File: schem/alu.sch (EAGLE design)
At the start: 10 parts, among them IC1 74HC181N, IC10 74HC08N, IC11 74HC86N, IC2 74HC181N, IC3 74HC04N, IC5 74HC244N, IC6 74HC244N, IC7 74HC32N, IC8 74HC32N, IC9 74HC86N

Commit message: updated alu schematic
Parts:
- added IC12, IC13, IC14, IC15, IC16, IC17: 74HC151N, 74xx-eu:74HC151N
- added IC18: 74HC244N, 74xx-eu:74HC244N
- added IC4: 74HC181N, 74xx-eu:74HC181N
- IC1: value 74HC181N -> 74HC244N; device 74xx-eu:74HC181N -> 74xx-eu:74HC244N
- IC11: value 74HC86N -> 74HC377N; device 74xx-eu:74HC86N -> 74xx-eu:74HC377N
- IC2: value 74HC181N -> 74HC04N; device 74xx-eu:74HC181N -> 74xx-eu:74HC04N
- IC3: value 74HC04N -> 74HC86N; device 74xx-eu:74HC04N -> 74xx-eu:74HC86N
- IC5: value 74HC244N -> 74HC181N; device 74xx-eu:74HC244N -> 74xx-eu:74HC181N
- IC7: value 74HC32N -> 74HC86N; device 74xx-eu:74HC32N -> 74xx-eu:74HC86N
- IC9: value 74HC86N -> 74HC32N; device 74xx-eu:74HC86N -> 74xx-eu:74HC32N
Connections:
- new net CLK: IC11A.CLK
- new net COND: IC17A.Y
- new net FL0: IC12A.A
- new net FL1: IC12A.B
- new net FL2: IC13A.A
- new net FL3: IC13A.B
- new net FL4: IC14A.A
- new net FL5: IC14A.B
- new net FL6: IC15A.A
- new net FL7: IC15A.B
- new net FL8: IC16A.A
- new net FL9: IC16A.B
- new net GND: IC11A.4D, IC11A.5D, IC11A.G, IC12A.D7, IC12A.G, IC13A.D7, IC13A.G, IC14A.D5, IC14A.D7, IC14A.G, IC15A.D7, IC15A.G, IC16A.D7, IC16A.G, IC17A.C, IC17A.D4, IC17A.D5, IC17A.D6, IC17A.D7, IC17A.G
- new net IBD10: IC18A.G, IC18B.G
- new net INIRQ: IC11A.6D
- new net N: IC16A.D5
- new net OBD10: IC12A.C, IC13A.C, IC14A.C, IC15A.C, IC16A.C
- new net PD0: IC11A.1D, IC12A.Y
- new net PD1: IC11A.2D, IC13A.Y
- new net PD2: IC11A.3D, IC14A.Y
- new net PD6: IC11A.7D, IC15A.Y
- new net PD7: IC11A.8D, IC16A.Y
- new net PQ0: IC11A.1Q, IC12A.D0, IC12A.D2, IC12A.D3, IC12A.D4, IC17A.D2, IC18A.A1
- new net PQ1: IC11A.2Q, IC13A.D0, IC13A.D2, IC13A.D3, IC13A.D4, IC17A.D3, IC18A.A2
- new net PQ2: IC11A.3Q, IC14A.D0, IC14A.D2, IC14A.D3, IC14A.D4, IC18A.A3
- new net PQ3: IC11A.4Q, IC18A.A4
- new net PQ4: IC11A.5Q, IC18B.A1
- new net PQ5: IC11A.6Q, IC18B.A2
- new net PQ6: IC11A.7Q, IC15A.D0, IC15A.D2, IC15A.D3, IC15A.D4, IC17A.D1, IC18B.A3
- new net PQ7: IC11A.8Q, IC16A.D0, IC16A.D2, IC16A.D3, IC16A.D4, IC17A.D0, IC18B.A4
- new net VCC: IC12A.D6, IC13A.D6, IC14A.D6, IC15A.D6, IC16A.D6
- net /CIN: now also IC2A.O, IC4A.CN; no longer IC1A.CN, IC3A.O
- net /COUTA: now also IC2B.I, IC5A.CN+4; no longer IC2A.CN+4, IC3B.I
- net /F0: now also IC2E.O, IC7A.I1; no longer IC3E.O, IC9A.I1
- net /F5: now also IC1A.G, IC1B.G, IC2C.O; no longer IC3C.O, IC6A.G, IC6B.G
- net /V1: now also IC2F.O; no longer IC3F.O
- net /Z: now also IC2D.I, IC8D.O; no longer IC3D.I, IC7D.O
- net C: now also IC12A.D5, IC9D.O; no longer IC8D.O
- net C1: now also IC9D.I0; no longer IC8D.I0
- net C2: now also IC9D.I1; no longer IC8D.I1
- net C4: now also IC4A.CN+4, IC5A.CN; no longer IC1A.CN+4, IC2A.CN
- net CIN: now also IC1B.A4, IC2A.I; no longer IC3A.I, IC6B.A4
- net COUTA: now also IC2B.O; no longer IC3B.O
- net DB0: now also IC4A.B0; no longer IC1A.B0
- net DB1: now also IC4A.B1; no longer IC1A.B1
- net DB2: now also IC4A.B2; no longer IC1A.B2
- net DB3: now also IC4A.B3; no longer IC1A.B3
- net DB4: now also IC5A.B0; no longer IC2A.B0
- net DB5: now also IC5A.B1; no longer IC2A.B1
- net DB6: now also IC17A.A, IC5A.B2; no longer IC2A.B2
- net DB7: now also IC17A.B, IC5A.B3, IC7A.I0; no longer IC2A.B3, IC9A.I0
- net F0: now also IC3A.I0; no longer IC11A.I0
- net F1: now also IC3B.I0; no longer IC11B.I0
- net F2: now also IC3C.I0; no longer IC11C.I0
- net F3: now also IC3D.I0; no longer IC11D.I0
- net F4: now also IC4A.M, IC5A.M; no longer IC1A.M, IC2A.M
- net F5: now also IC2C.I, IC6A.G, IC6B.G; no longer IC3C.I, IC5A.G, IC5B.G
- net FX0: now also IC2E.I, IC3A.O, IC4A.S0, IC5A.S0; no longer IC11A.O, IC1A.S0, IC2A.S0, IC3E.I
- net FX1: now also IC3B.O, IC4A.S1, IC5A.S1; no longer IC11B.O, IC1A.S1, IC2A.S1
- net FX2: now also IC3C.O, IC4A.S2, IC5A.S2; no longer IC11C.O, IC1A.S2, IC2A.S2
- net FX3: now also IC3D.O, IC4A.S3, IC5A.S3; no longer IC11D.O, IC1A.S3, IC2A.S3
- net IB0: now also IC18A.Y1, IC4A.A0; no longer IC1A.A0
- net IB1: now also IC18A.Y2, IC4A.A1; no longer IC6A.A1
- net IB2: now also IC18A.Y3, IC4A.A2; no longer IC6A.A2
- net IB3: now also IC18A.Y4, IC4A.A3; no longer IC6A.A3
- net IB4: now also IC18B.Y1, IC1A.A4, IC5A.A0; no longer IC2A.A0, IC6A.A4
- net IB5: now also IC18B.Y2, IC1B.A1, IC5A.A1; no longer IC2A.A1, IC6B.A1
- net IB6: now also IC18B.Y3, IC1B.A2, IC5A.A2; no longer IC2A.A2, IC6B.A2
- net IB7: now also IC18B.Y4, IC1B.A3, IC5A.A3, IC7B.I0, IC7C.I1; no longer IC2A.A3, IC6B.A3, IC9B.I0, IC9C.I1
- net INVF: now also IC3A.I1, IC3B.I1, IC3C.I1, IC3D.I1; no longer IC11A.I1, IC11B.I1, IC11C.I1, IC11D.I1
- net OB0: now also IC12A.D1, IC1A.Y1, IC8A.I0; no longer IC5A.Y1, IC7A.I0
- net OB1: now also IC13A.D1, IC1A.Y2, IC8A.I1; no longer IC5A.Y2, IC7A.I1
- net OB2: now also IC14A.D1, IC1A.Y3, IC8B.I0; no longer IC5A.Y3, IC7B.I0
- net OB3: now also IC1A.Y4, IC8B.I1; no longer IC5A.Y4, IC7B.I1
- net OB4: now also IC1B.Y1, IC9A.I0; no longer IC5B.Y1, IC8A.I0
- net OB5: now also IC1B.Y2, IC9A.I1; no longer IC5B.Y2, IC8A.I1
- net OB6: now also IC15A.D1, IC1B.Y3, IC9B.I0; no longer IC5B.Y3, IC8B.I0
- net OB7: now also IC16A.D1, IC1B.Y4, IC9B.I1; no longer IC5B.Y4, IC8B.I1
- net OBA0: now also IC4A.F0, IC6A.A1; no longer IC1A.F0, IC5A.A1
- net OBA1: now also IC4A.F1, IC6A.A2; no longer IC1A.F1, IC5A.A2
- net OBA2: now also IC4A.F2, IC6A.A3; no longer IC1A.F2, IC5A.A3
- net OBA3: now also IC4A.F3, IC6A.A4; no longer IC1A.F3, IC5A.A4
- net OBA4: now also IC5A.F0, IC6B.A1; no longer IC2A.F0, IC5B.A1
- net OBA5: now also IC5A.F1, IC6B.A2; no longer IC2A.F1, IC5B.A2
- net OBA6: now also IC5A.F2, IC6B.A3; no longer IC2A.F2, IC5B.A3
- net OBA7: now also IC5A.F3, IC6B.A4, IC7C.I0; no longer IC2A.F3, IC5B.A4, IC9C.I0
- net V: now also IC15A.D5
- net V0: now also IC7A.O, IC7B.I1; no longer IC9A.O, IC9B.I1
- net V1: now also IC2F.I, IC7B.O; no longer IC3F.I, IC9B.O
- net V2: now also IC7C.O; no longer IC9C.O
- net Z: now also IC13A.D5, IC2D.O; no longer IC3D.O
- net Z0: now also IC8A.O, IC8C.I0; no longer IC7A.O, IC7C.I0
- net Z1: now also IC8B.O, IC8C.I1; no longer IC7B.O, IC7C.I1
- net Z2: now also IC9A.O, IC9C.I0; no longer IC8A.O, IC8C.I0
- net Z3: now also IC9B.O, IC9C.I1; no longer IC8B.O, IC8C.I1
- net Z4: now also IC8C.O, IC8D.I0; no longer IC7C.O, IC7D.I0
- net Z5: now also IC8D.I1, IC9C.O; no longer IC7D.I1, IC8C.O
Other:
- moved on the sheet: IC6A, IC6B, IC8A, IC8B, IC8C, IC8D

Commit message: rom and misc board schematics
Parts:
- IC1: value 74HC244N -> 74HC181N; device 74xx-eu:74HC244N -> 74xx-eu:74HC181N
- IC11: value 74HC377N -> 74HC151N; device 74xx-eu:74HC377N -> 74xx-eu:74HC151N
- IC14: value 74HC151N -> 74HC244N; device 74xx-eu:74HC151N -> 74xx-eu:74HC244N
- IC18: value 74HC244N -> 74HC377N; device 74xx-eu:74HC244N -> 74xx-eu:74HC377N
- IC2: value 74HC04N -> 74HC181N; device 74xx-eu:74HC04N -> 74xx-eu:74HC181N
- IC3: value 74HC86N -> 74HC04N; device 74xx-eu:74HC86N -> 74xx-eu:74HC04N
- IC4: value 74HC181N -> 74HC244N; device 74xx-eu:74HC181N -> 74xx-eu:74HC244N
- IC5: value 74HC181N -> 74HC32N; device 74xx-eu:74HC181N -> 74xx-eu:74HC32N
- IC6: value 74HC244N -> 74HC86N; device 74xx-eu:74HC244N -> 74xx-eu:74HC86N
- IC8: value 74HC32N -> 74HC244N; device 74xx-eu:74HC32N -> 74xx-eu:74HC244N
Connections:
- net /CIN: now also IC1A.CN, IC3A.O; no longer IC2A.O, IC4A.CN
- net /COUTA: now also IC2A.CN+4, IC3B.I; no longer IC2B.I, IC5A.CN+4
- net /F0: now also IC3E.O, IC6A.I1; no longer IC2E.O, IC7A.I1
- net /F5: now also IC3C.O, IC8A.G, IC8B.G; no longer IC1A.G, IC1B.G, IC2C.O
- net /V1: now also IC3F.O; no longer IC2F.O
- net /Z: now also IC3D.I, IC5D.O; no longer IC2D.I, IC8D.O
- net C: now also IC11A.D5; no longer IC12A.D5
- net C4: now also IC1A.CN+4, IC2A.CN; no longer IC4A.CN+4, IC5A.CN
- net CIN: now also IC3A.I, IC8B.A4; no longer IC1B.A4, IC2A.I
- net CLK: now also IC18A.CLK; no longer IC11A.CLK
- net COUTA: now also IC3B.O; no longer IC2B.O
- net DB0: now also IC1A.B0; no longer IC4A.B0
- net DB1: now also IC1A.B1; no longer IC4A.B1
- net DB2: now also IC1A.B2; no longer IC4A.B2
- net DB3: now also IC1A.B3; no longer IC4A.B3
- net DB4: now also IC2A.B0; no longer IC5A.B0
- net DB5: now also IC2A.B1; no longer IC5A.B1
- net DB6: now also IC2A.B2; no longer IC5A.B2
- net DB7: now also IC2A.B3, IC6A.I0; no longer IC5A.B3, IC7A.I0
- net F0: now also IC7A.I0; no longer IC3A.I0
- net F1: now also IC7B.I0; no longer IC3B.I0
- net F2: now also IC7C.I0; no longer IC3C.I0
- net F3: now also IC7D.I0; no longer IC3D.I0
- net F4: now also IC1A.M, IC2A.M; no longer IC4A.M, IC5A.M
- net F5: now also IC3C.I, IC4A.G, IC4B.G; no longer IC2C.I, IC6A.G, IC6B.G
- net FL0: now also IC11A.A; no longer IC12A.A
- net FL1: now also IC11A.B; no longer IC12A.B
- net FL2: now also IC12A.A; no longer IC13A.A
- net FL3: now also IC12A.B; no longer IC13A.B
- net FL4: now also IC13A.A; no longer IC14A.A
- net FL5: now also IC13A.B; no longer IC14A.B
- net FX0: now also IC1A.S0, IC2A.S0, IC3E.I, IC7A.O; no longer IC2E.I, IC3A.O, IC4A.S0, IC5A.S0
- net FX1: now also IC1A.S1, IC2A.S1, IC7B.O; no longer IC3B.O, IC4A.S1, IC5A.S1
- net FX2: now also IC1A.S2, IC2A.S2, IC7C.O; no longer IC3C.O, IC4A.S2, IC5A.S2
- net FX3: now also IC1A.S3, IC2A.S3, IC7D.O; no longer IC3D.O, IC4A.S3, IC5A.S3
- net GND: now also IC11A.D7, IC13A.D5, IC18A.4D, IC18A.5D, IC18A.G; no longer IC11A.4D, IC11A.5D, IC14A.D5, IC14A.D7, IC14A.G
- net IB0: now also IC14A.Y1, IC1A.A0; no longer IC18A.Y1, IC4A.A0
- net IB1: now also IC14A.Y2, IC8A.A1; no longer IC18A.Y2, IC4A.A1
- net IB2: now also IC14A.Y3, IC8A.A2; no longer IC18A.Y3, IC4A.A2
- net IB3: now also IC14A.Y4, IC8A.A3; no longer IC18A.Y4, IC4A.A3
- net IB4: now also IC14B.Y1, IC2A.A0, IC8A.A4; no longer IC18B.Y1, IC1A.A4, IC5A.A0
- net IB5: now also IC14B.Y2, IC2A.A1, IC8B.A1; no longer IC18B.Y2, IC1B.A1, IC5A.A1
- net IB6: now also IC14B.Y3, IC2A.A2, IC8B.A2; no longer IC18B.Y3, IC1B.A2, IC5A.A2
- net IB7: now also IC14B.Y4, IC2A.A3, IC6B.I0, IC6C.I1, IC8B.A3; no longer IC18B.Y4, IC1B.A3, IC5A.A3, IC7B.I0, IC7C.I1
- net IBD10: now also IC14A.G, IC14B.G; no longer IC18A.G, IC18B.G
- net INIRQ: now also IC18A.6D; no longer IC11A.6D
- net INVF: now also IC7A.I1, IC7B.I1, IC7C.I1, IC7D.I1; no longer IC3A.I1, IC3B.I1, IC3C.I1, IC3D.I1
- net OB0: now also IC11A.D1, IC4A.Y1, IC5A.I0, IC8A.Y1; no longer IC12A.D1, IC1A.Y1, IC6A.Y1, IC8A.I0
- net OB1: now also IC12A.D1, IC4A.Y2, IC5A.I1, IC8A.Y2; no longer IC13A.D1, IC1A.Y2, IC6A.Y2, IC8A.I1
- net OB2: now also IC13A.D1, IC4A.Y3, IC5B.I0, IC8A.Y3; no longer IC14A.D1, IC1A.Y3, IC6A.Y3, IC8B.I0
- net OB3: now also IC4A.Y4, IC5B.I1, IC8A.Y4; no longer IC1A.Y4, IC6A.Y4, IC8B.I1
- net OB4: now also IC4B.Y1, IC8B.Y1; no longer IC1B.Y1, IC6B.Y1
- net OB5: now also IC4B.Y2, IC8B.Y2; no longer IC1B.Y2, IC6B.Y2
- net OB6: now also IC4B.Y3, IC8B.Y3; no longer IC1B.Y3, IC6B.Y3
- net OB7: now also IC4B.Y4, IC8B.Y4; no longer IC1B.Y4, IC6B.Y4
- net OBA0: now also IC1A.F0, IC4A.A1; no longer IC4A.F0, IC6A.A1
- net OBA1: now also IC1A.F1, IC4A.A2; no longer IC4A.F1, IC6A.A2
- net OBA2: now also IC1A.F2, IC4A.A3; no longer IC4A.F2, IC6A.A3
- net OBA3: now also IC1A.F3, IC4A.A4; no longer IC4A.F3, IC6A.A4
- net OBA4: now also IC2A.F0, IC4B.A1; no longer IC5A.F0, IC6B.A1
- net OBA5: now also IC2A.F1, IC4B.A2; no longer IC5A.F1, IC6B.A2
- net OBA6: now also IC2A.F2, IC4B.A3; no longer IC5A.F2, IC6B.A3
- net OBA7: now also IC2A.F3, IC4B.A4, IC6C.I0; no longer IC5A.F3, IC6B.A4, IC7C.I0
- net OBD10: now also IC11A.C; no longer IC14A.C
- net PD0: now also IC11A.Y, IC18A.1D; no longer IC11A.1D, IC12A.Y
- net PD1: now also IC12A.Y, IC18A.2D; no longer IC11A.2D, IC13A.Y
- net PD2: now also IC13A.Y, IC18A.3D; no longer IC11A.3D, IC14A.Y
- net PD6: now also IC18A.7D; no longer IC11A.7D
- net PD7: now also IC18A.8D; no longer IC11A.8D
- net PQ0: now also IC11A.D0, IC11A.D2, IC11A.D3, IC11A.D4, IC14A.A1, IC18A.1Q; no longer IC11A.1Q, IC12A.D0, IC12A.D2, IC12A.D3, IC12A.D4, IC18A.A1
- net PQ1: now also IC12A.D0, IC12A.D2, IC12A.D3, IC12A.D4, IC14A.A2, IC18A.2Q; no longer IC11A.2Q, IC13A.D0, IC13A.D2, IC13A.D3, IC13A.D4, IC18A.A2
- net PQ2: now also IC13A.D0, IC13A.D2, IC13A.D3, IC13A.D4, IC14A.A3, IC18A.3Q; no longer IC11A.3Q, IC14A.D0, IC14A.D2, IC14A.D3, IC14A.D4, IC18A.A3
- net PQ3: now also IC14A.A4, IC18A.4Q; no longer IC11A.4Q, IC18A.A4
- net PQ4: now also IC14B.A1, IC18A.5Q; no longer IC11A.5Q, IC18B.A1
- net PQ5: now also IC14B.A2, IC18A.6Q; no longer IC11A.6Q, IC18B.A2
- net PQ6: now also IC14B.A3, IC18A.7Q; no longer IC11A.7Q, IC18B.A3
- net PQ7: now also IC14B.A4, IC18A.8Q; no longer IC11A.8Q, IC18B.A4
- net V0: now also IC6A.O, IC6B.I1; no longer IC7A.O, IC7B.I1
- net V1: now also IC3F.I, IC6B.O; no longer IC2F.I, IC7B.O
- net V2: now also IC6C.O; no longer IC7C.O
- net VCC: now also IC11A.D6; no longer IC14A.D6
- net Z: now also IC12A.D5, IC3D.O; no longer IC13A.D5, IC2D.O
- net Z0: now also IC5A.O, IC5C.I0; no longer IC8A.O, IC8C.I0
- net Z1: now also IC5B.O, IC5C.I1; no longer IC8B.O, IC8C.I1
- net Z4: now also IC5C.O, IC5D.I0; no longer IC8C.O, IC8D.I0
- net Z5: now also IC5D.I1; no longer IC8D.I1
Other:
- moved on the sheet: IC12, IC13, IC7A, IC7B, IC7C

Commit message: progress
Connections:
- net C renamed ALUC
- removed net N: IC16A.D5
- net OB7: now also IC16A.D5
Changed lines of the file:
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@@
 <label x="299.72" y="48.26" size="1.778" layer="95"/>
+</segment>
+<segment>
+<pinref part="IC16" gate="A" pin="D5"/>
+<wire x1="304.8" y1="38.1" x2="299.72" y2="38.1" width="0.1524" layer="91"/>
+<label x="299.72" y="38.1" size="1.778" layer="95"/>
 </segment>
 </net>
@@
 </segment>
 </net>
-<net name="C" class="0">
+<net name="ALUC" class="0">
 <segment>
 <pinref part="IC9" gate="D" pin="O"/>
@@
 </segment>
 </net>
-<net name="N" class="0">
-<segment>
-<pinref part="IC16" gate="A" pin="D5"/>
-<wire x1="304.8" y1="38.1" x2="299.72" y2="38.1" width="0.1524" layer="91"/>
-<label x="299.72" y="38.1" size="1.778" layer="95"/>
-</segment>
-</net>
 <net name="FL8" class="0">
 <segment>
@@
 </sheet>
 </sheets>
+<errors>
+</errors>
 </schematic>
 </drawing>

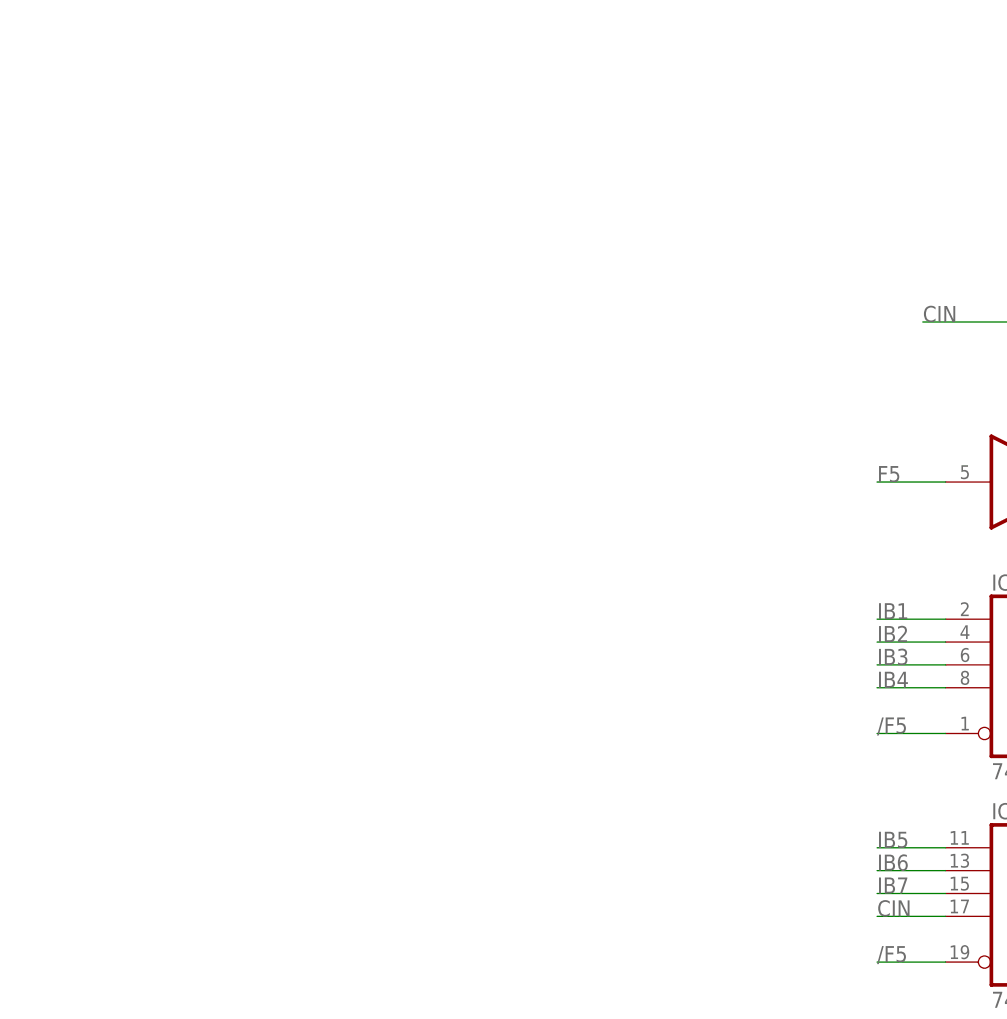
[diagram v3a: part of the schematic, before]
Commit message: connector layout changes
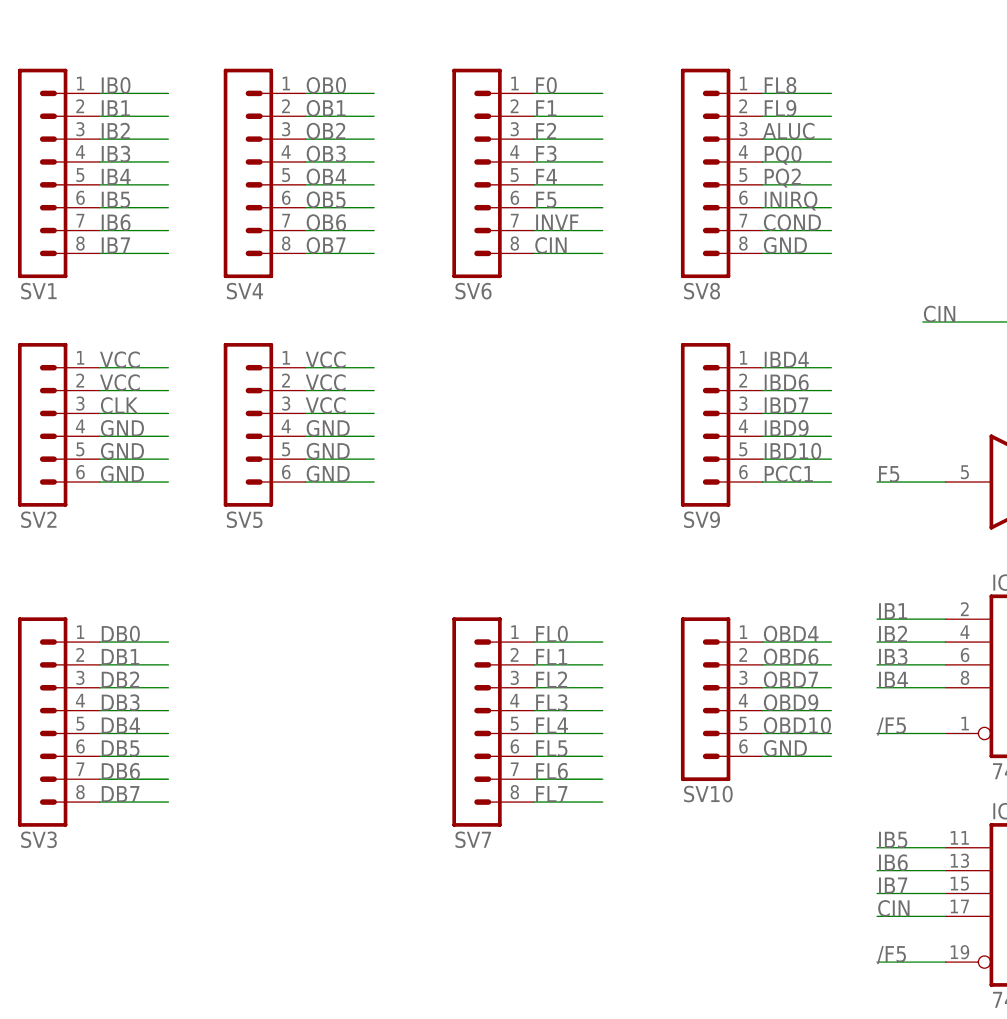
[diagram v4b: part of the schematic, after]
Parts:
- added SV1, SV3, SV4, SV6, SV7, SV8: (no value), con-lstb:MA08-1
- added SV10, SV2, SV5, SV9: (no value), con-lstb:MA06-1
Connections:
- new net IBD4: SV9.1
- new net IBD6: SV9.2
- new net IBD7: SV9.3
- new net IBD9: SV9.4
- new net OBD4: SV10.1
- new net OBD6: SV10.2
- new net OBD7: SV10.3
- new net OBD9: SV10.4
- new net PCC1: SV9.6
- net ALUC: now also SV8.3
- net CIN: now also SV6.8
- net CLK: now also SV2.3
- net COND: now also SV8.7
- net DB0: now also SV3.1
- net DB1: now also SV3.2
- net DB2: now also SV3.3
- net DB3: now also SV3.4
- net DB4: now also SV3.5
- net DB5: now also SV3.6
- net DB6: now also SV3.7
- net DB7: now also SV3.8
- net F0: now also SV6.1
- net F1: now also SV6.2
- net F2: now also SV6.3
- net F3: now also SV6.4
- net F4: now also SV6.5
- net F5: now also SV6.6
- net FL0: now also SV7.1
- net FL1: now also SV7.2
- net FL2: now also SV7.3
- net FL3: now also SV7.4
- net FL4: now also SV7.5
- net FL5: now also SV7.6
- net FL6: now also SV7.7
- net FL7: now also SV7.8
- net FL8: now also SV8.1
- net FL9: now also SV8.2
- net GND: now also SV10.6, SV2.4, SV2.5, SV2.6, SV5.4, SV5.5, SV5.6, SV8.8
- net IB0: now also SV1.1
- net IB1: now also SV1.2
- net IB2: now also SV1.3
- net IB3: now also SV1.4
- net IB4: now also SV1.5
- net IB5: now also SV1.6
- net IB6: now also SV1.7
- net IB7: now also SV1.8
- net IBD10: now also SV9.5
- net INIRQ: now also SV8.6
- net INVF: now also SV6.7
- net OB0: now also SV4.1
- net OB1: now also SV4.2
- net OB2: now also SV4.3
- net OB3: now also SV4.4
- net OB4: now also SV4.5
- net OB5: now also SV4.6
- net OB6: now also SV4.7
- net OB7: now also SV4.8
- net OBD10: now also SV10.5
- net PQ0: now also SV8.4
- net PQ2: now also SV8.5
- net VCC: now also SV2.1, SV2.2, SV5.1, SV5.2, SV5.3

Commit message: board changes ; rom schematic finished
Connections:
- net GND: now also IC10D.I0, IC10D.I1, IC6D.I0, IC6D.I1
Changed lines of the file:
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@@
 <part name="SV9" library="con-lstb" deviceset="MA06-1" device=""/>
 <part name="SV10" library="con-lstb" deviceset="MA06-1" device=""/>
+<part name="GND2" library="supply1" deviceset="GND" device=""/>
+<part name="GND3" library="supply1" deviceset="GND" device=""/>
 </parts>
 <sheets>
@@
 <instance part="SV9" gate="1" x="-15.24" y="53.34" rot="MR180"/>
 <instance part="SV10" gate="1" x="-15.24" y="22.86" rot="MR180"/>
+<instance part="IC10" gate="D" x="190.5" y="-15.24"/>
+<instance part="GND2" gate="1" x="182.88" y="-20.32"/>
+<instance part="IC6" gate="D" x="218.44" y="-15.24"/>
+<instance part="GND3" gate="1" x="210.82" y="-20.32"/>
 </instances>
 <busses>
@@
 <label x="-7.62" y="17.78" size="1.778" layer="95"/>
 </segment>
-</net>
+<segment>
+<pinref part="IC10" gate="D" pin="I0"/>
+<pinref part="IC10" gate="D" pin="I1"/>
+<wire x1="182.88" y1="-12.7" x2="182.88" y2="-17.78" width="0.1524" layer="91"/>
+<pinref part="GND2" gate="1" pin="GND"/>
+<junction x="182.88" y="-17.78"/>
+</segment>
+<segment>
+<pinref part="IC6" gate="D" pin="I0"/>
+<pinref part="IC6" gate="D" pin="I1"/>
+<wire x1="210.82" y1="-12.7" x2="210.82" y2="-17.78" width="0.1524" layer="91"/>
+<pinref part="GND3" gate="1" pin="GND"/>
+<junction x="210.82" y="-17.78"/>
+</segment>
+</net>
